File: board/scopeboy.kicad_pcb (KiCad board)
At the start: 4 copper layers, 100 x 80 mm, 151 parts, among them J1 USB_C_Receptacle_USB2.0_16P, J2 SM03B-SRSS-TB, J3 SM03B-SRSS-TB, J4 Conn_01x10, J5 SM04B-SRSS-TB, J6 HDMI_A, J7 731000105, J8 Conn_01x02, J9 Conn_01x08, SW1 SW_Push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

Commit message: Updated the board stackup
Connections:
- C1 pad 1: +3V3 -> +3.3V
- C13 pad 1: +3V3 -> +3.3V
- C14 pad 1: +3V3 -> +3.3V
- C15 pad 1: +3V3 -> +3.3V
- C16 pad 1: +3V3 -> +3.3V
- C17 pad 1: +3V3 -> +3.3V
- C18 pad 1: +3V3 -> +3.3V
- C19 pad 1: +3V3 -> +3.3V
- C2 pad 1: +3V3 -> +3.3V
- C20 pad 1: +3V3 -> +3.3V
- C21 pad 1: +3V3 -> +3.3V
- C22 pad 1: +3V3 -> +3.3V
- C36 pad 2: +3V3 -> +3.3V
- C38 pad 2: +3V3 -> +3.3V
- C5 pad 1: +3V3 -> +3.3V
- J4 pad 2: +3V3 -> +3.3V
- J5 pad 2: +3V3 -> +3.3V
- R10 pad 1: +3V3 -> +3.3V
- R14 pad 2: +3V3 -> +3.3V
- R15 pad 2: +3V3 -> +3.3V
- R4 pad 1: +3V3 -> +3.3V
- R5 pad 1: +3V3 -> +3.3V
- U1 pad 8: +3V3 -> +3.3V
- U2 pad 8: +3V3 -> +3.3V
- U4 pad 15: +3V3 -> +3.3V
- U4 pad 24: +3V3 -> +3.3V
- U4 pad 27: /GPIO26 -> /Backlight
- U4 pad 28: /GPIO27 -> /D/C
- U4 pad 29: +3V3 -> +3.3V
- U4 pad 41: +3V3 -> +3.3V
- U4 pad 5: +3V3 -> +3.3V
- U4 pad 50: +3V3 -> +3.3V
- U4 pad 59: +3V3 -> +3.3V
- U4 pad 60: +3V3 -> +3.3V
- U4 pad 64: +3V3 -> +3.3V
- U4 pad 68: +3V3 -> +3.3V
- U4 pad 69: +3V3 -> +3.3V
- U4 pad 76: +3V3 -> +3.3V
- U7 pad 18: +3V3 -> +3.3V
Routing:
- net +3V3: track 43.7 -> 0.00 mm
- net +3.3V: track 0.00 -> 43.7 mm
- added copper zone on F.Cu, net +3.3V
- added copper zone on In2.Cu, net +3.3V
- removed copper zone on F.Cu, net +3V3
- removed copper zone on In2.Cu, net +3V3

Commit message: Production version of board
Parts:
- moved R29 191.1 mm to (197.7, 115.9), turned to 90 degrees
- moved R28 190.9 mm to (196.0, 115.9), turned to 90 degrees
- moved C37 185.6 mm to (211.9, 129.3), turned to 180 degrees
- moved R25 184.3 mm to (193.8, 111.3), turned to 90 degrees
- moved R24 184.0 mm to (192.1, 111.3), turned to 90 degrees
- moved R30 178.4 mm to (193.0, 99.9), turned to -90 degrees
- moved R26 177.7 mm to (190.1, 105.7)
- moved R27 177.3 mm to (190.1, 107.3)
- moved R31 175.8 mm to (191.3, 99.9), turned to -90 degrees
- moved R20 164.6 mm to (169.5, 102.2), turned to -90 degrees
- moved R6 164.2 mm to (198.4, 85.8)
- moved R7 163.4 mm to (198.8, 80.0)
- moved R32 161.8 mm to (183.9, 83.5), turned to 180 degrees
- moved R22 149.5 mm to (167.1, 77.6)
- moved R23 148.9 mm to (166.7, 79.6)
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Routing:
- net GND: track 20.4 -> 272.2 mm, vias 5 -> 56
- net VDC: track 0.00 -> 125.3 mm
- net /SWD: track 0.00 -> 116.3 mm
- net -3V3: track 0.00 -> 101.6 mm, vias 0 -> 5
- net /SWCLK: track 0.00 -> 94.5 mm
- net +3.3V: track 43.7 -> 133.3 mm, vias 0 -> 26
- net /SD_D0: track 0.00 -> 88.8 mm, vias 0 -> 1
- net GNDA: track 5.72 -> 93.1 mm, vias 0 -> 32
- net /TX: track 0.00 -> 84.8 mm, vias 0 -> 2
- net /SCL: track 0.00 -> 82.7 mm, vias 0 -> 6
- net /CSSD: track 0.00 -> 80.9 mm, vias 0 -> 1
- net /DISD: track 0.00 -> 80.7 mm, vias 0 -> 1
- net /RX: track 0.00 -> 80.5 mm, vias 0 -> 2
- net /MISO: track 0.28 -> 75.5 mm, vias 0 -> 3
- net /D2: track 0.00 -> 72.8 mm, vias 0 -> 2
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- added copper zone on In2.Cu, net +3.3VA
- added copper zone on In1.Cu, net GND
- removed copper zone on F.Cu, net +1V1
- removed copper zone on F.Cu, net +3.3V
- removed copper zone on In2.Cu, net -3V3
- removed copper zone on F.Cu, net /VREG_LX
- removed copper zone on B.Cu, net GND
- removed copper zone on F.Cu, net GND
- removed copper zone on B.Cu, net GNDA
- removed copper zone on F.Cu, net GNDA
- removed copper zone on F.Cu, net VBUS
- removed copper zone on In2.Cu, net VBUS
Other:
- rule pad_to_mask_clearance: 0.03 -> 0

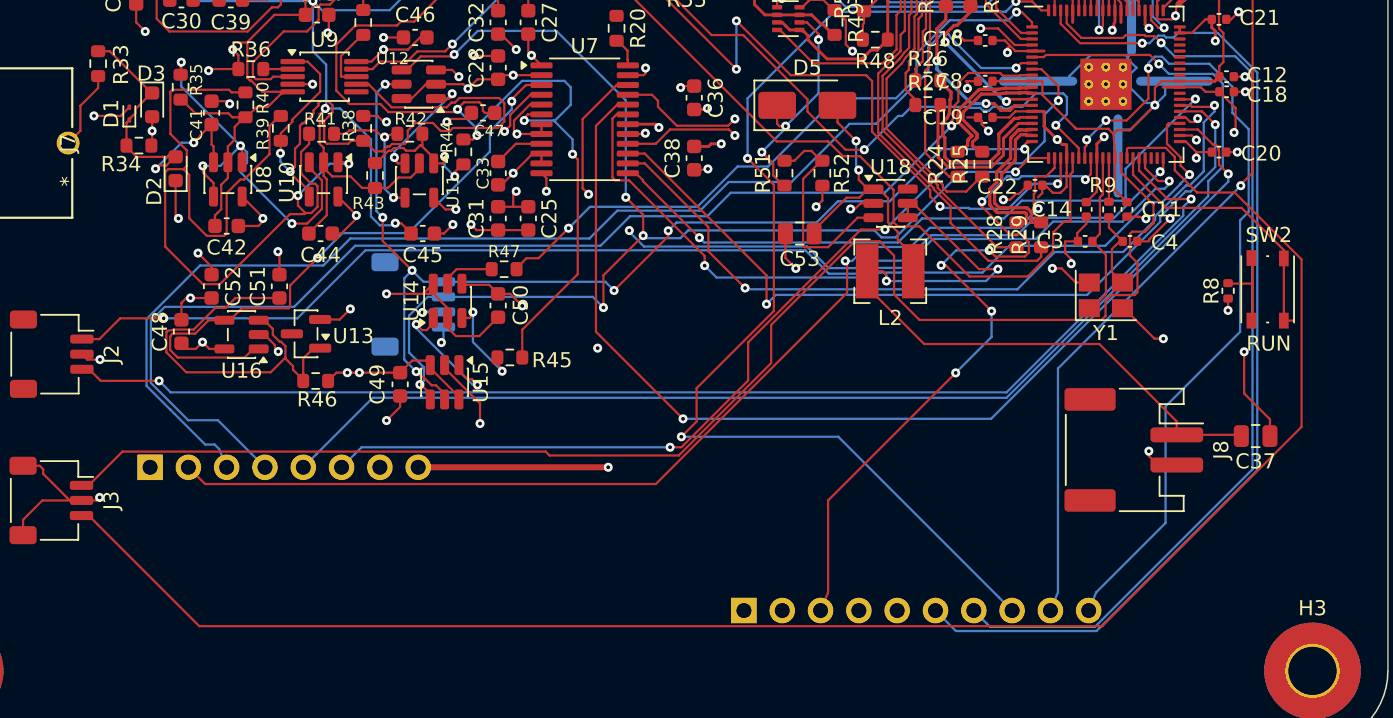
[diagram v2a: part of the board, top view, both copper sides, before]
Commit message: Fixing reset on TFT
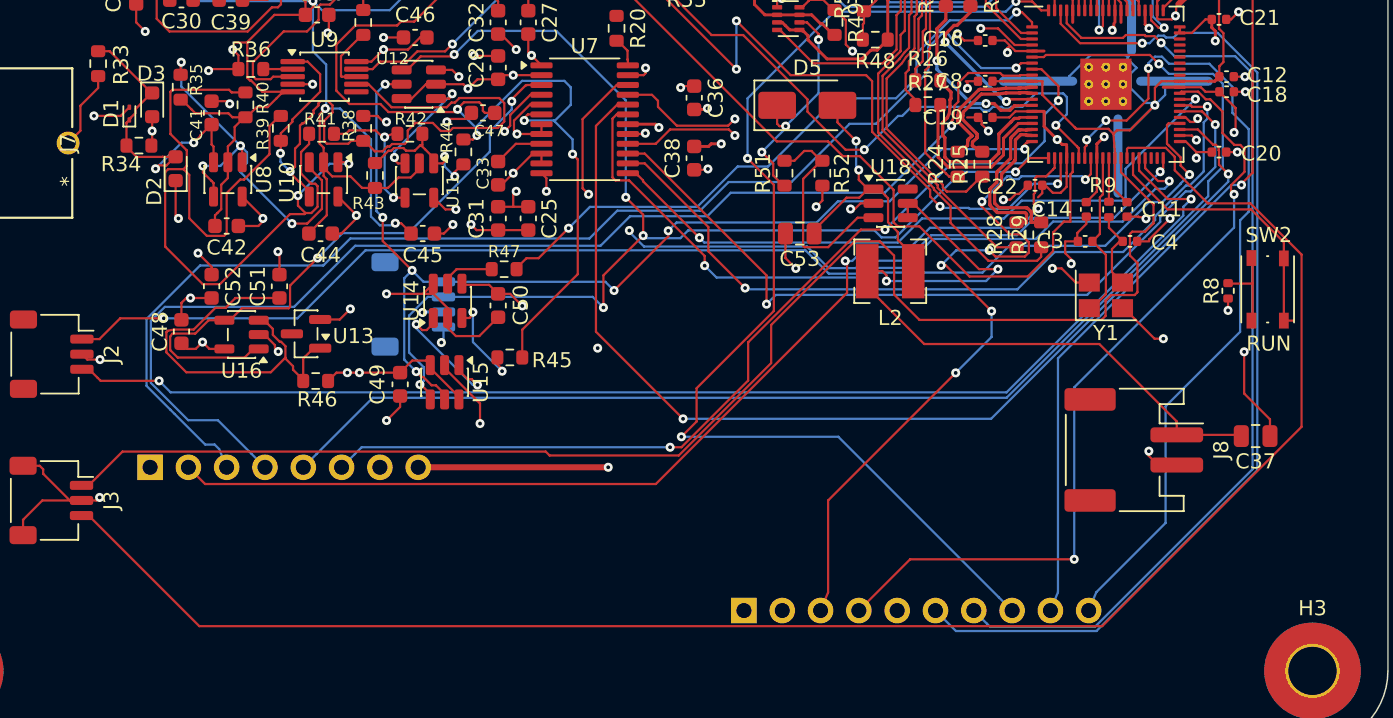
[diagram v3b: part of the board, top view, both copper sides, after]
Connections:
- U4 pad 38: /GPIO30 -> unconnected-(U4-GPIO30-Pad38)
- U4 pad 49: /GPIO40_ADC0 -> /Reset
- U4 pad 52: /GPIO41_ADC1 -> unconnected-(U4-GPIO41_ADC1-Pad52)
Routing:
- net /Reset: track 0.00 -> 54.5 mm, vias 0 -> 2
- net /D6: track 53.0 -> 52.3 mm
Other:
- board text added: "ScopeBoy Designed by: Robbie Leslie, Immanuel Koshy Cornell University Department of Electrical and Computer Engineering V1.1"
- board text removed: "ScopeBoy Designed by: Robbie Leslie, Immanuel Koshy Cornell University Department of Electrical and Computer Engineering"

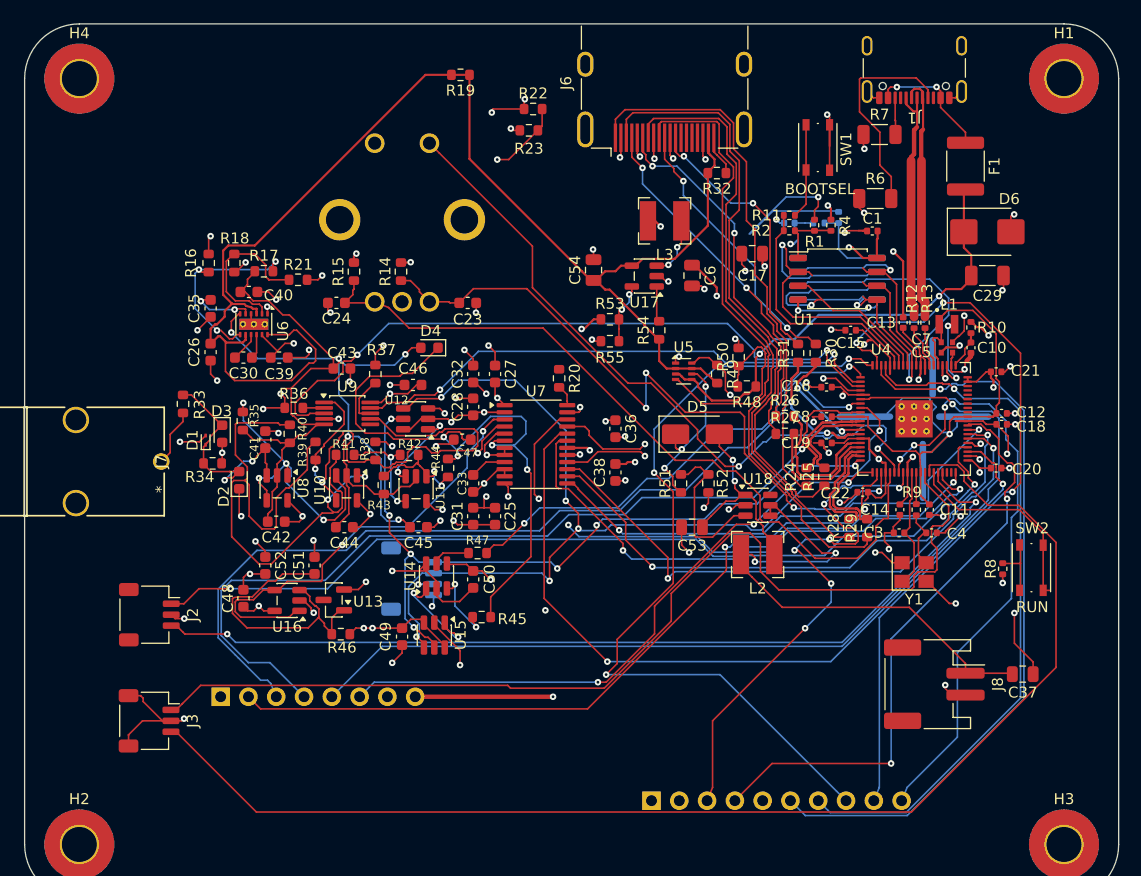
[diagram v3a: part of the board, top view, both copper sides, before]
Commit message: Fixed joystick qwiic connector bug
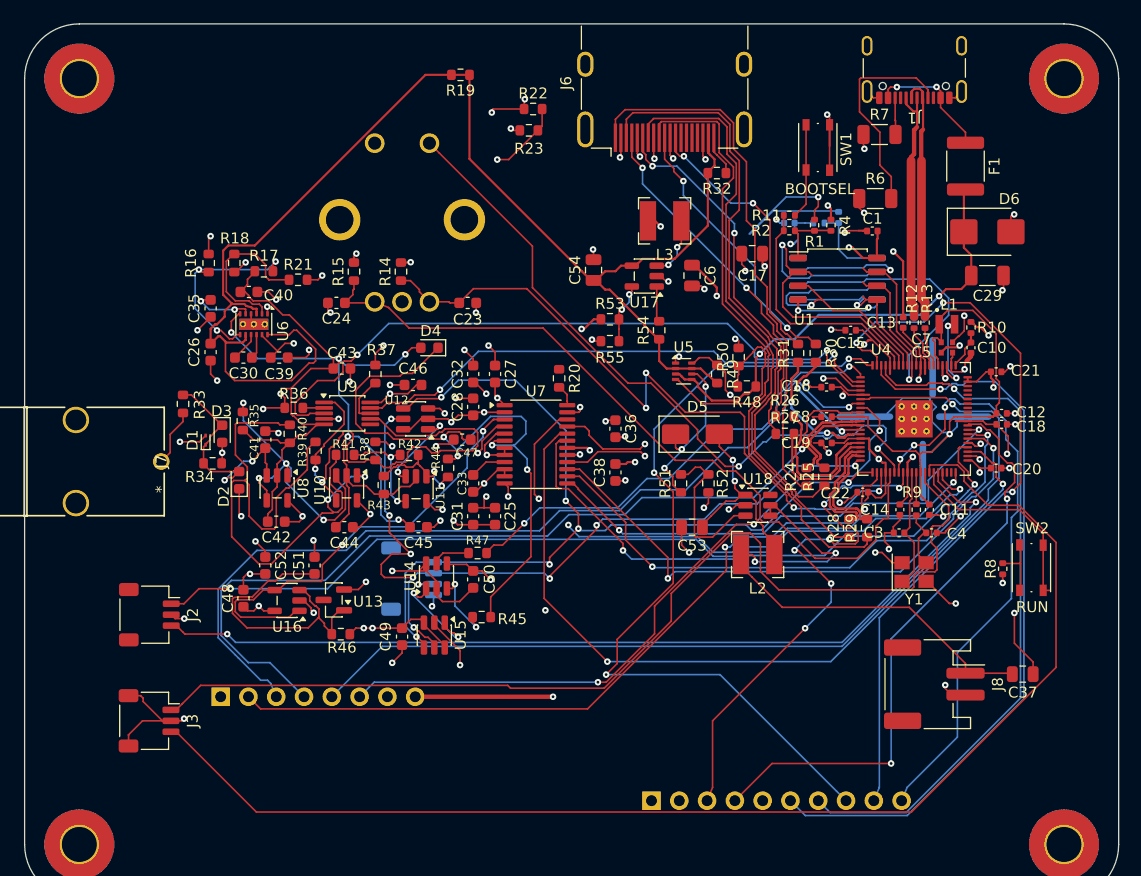
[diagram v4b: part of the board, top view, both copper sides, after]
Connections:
- J5 pad 3: /SCL -> /SDA
- J5 pad 4: /SDA -> /SCL
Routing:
- net /SDA: track 70.9 -> 75.7 mm, vias 7 -> 8

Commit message: Started work on fixing PCB bugs
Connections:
- R20 pad 1: CLK -> /ADC_CLK
- U12 pad 4: /SCL -> /SDA
- U12 pad 5: /SDA -> /SCL
- U15 pad 4: /SCL -> /SDA
- U15 pad 5: /SDA -> /SCL
- U4 pad 39: /GPIO31 -> /PowerStatus
- U4 pad 4: /PowerStatus -> /ADC_CLK
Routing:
- net /ADC_CLK: track 0.00 -> 13.1 mm, vias 0 -> 1
- net /PowerStatus: track 19.3 -> 21.8 mm
- net /D0: track 52.7 -> 53.3 mm
- net /RX: track 80.5 -> 79.9 mm
